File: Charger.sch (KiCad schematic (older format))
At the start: 7 parts

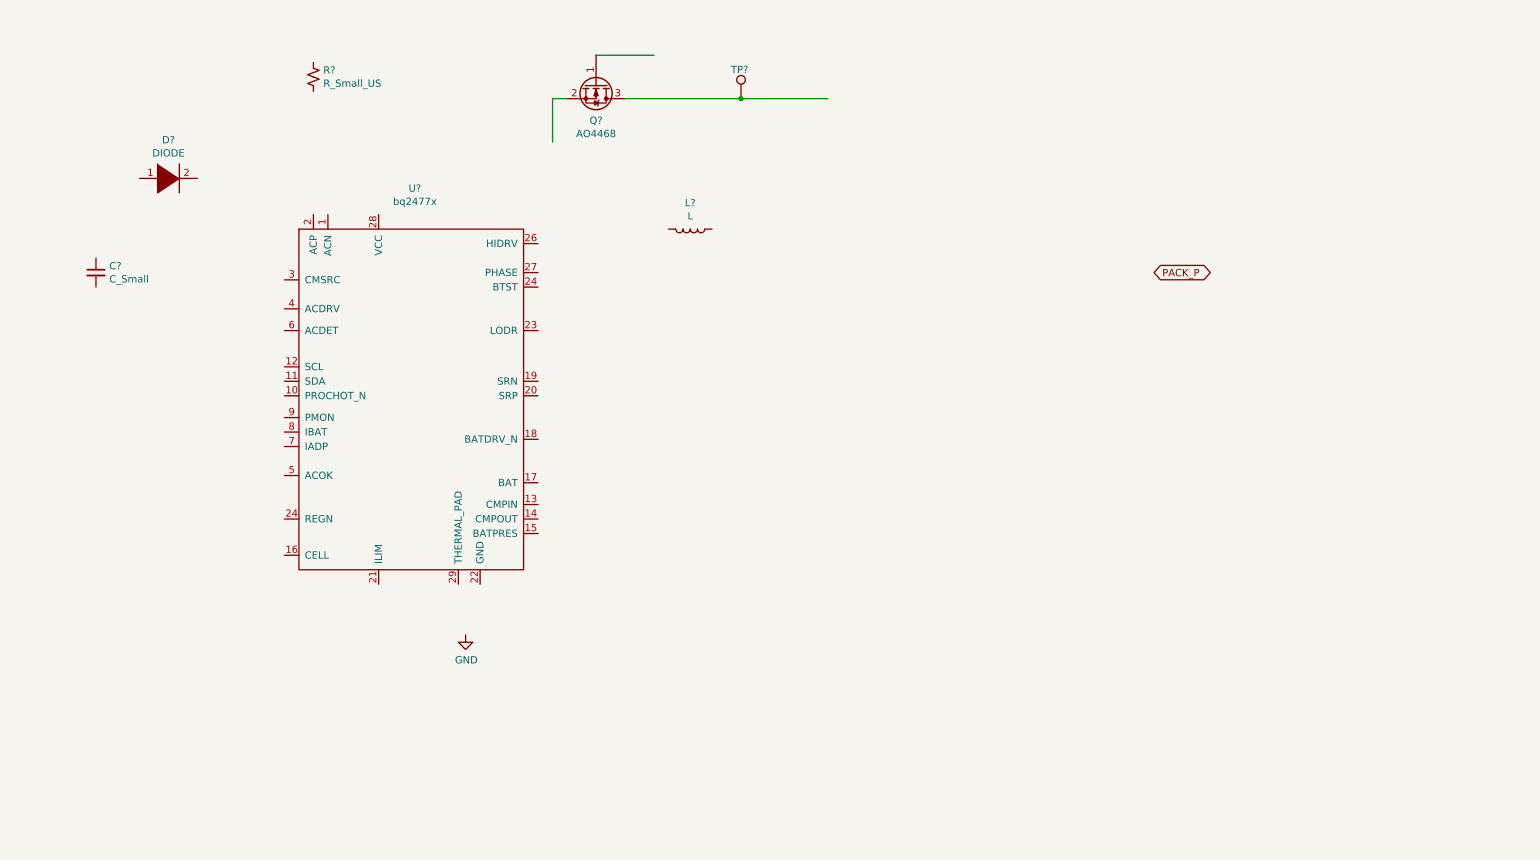
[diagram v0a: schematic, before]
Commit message: Added capacitors, inductors to charger page. Fixed capacitor sizes.
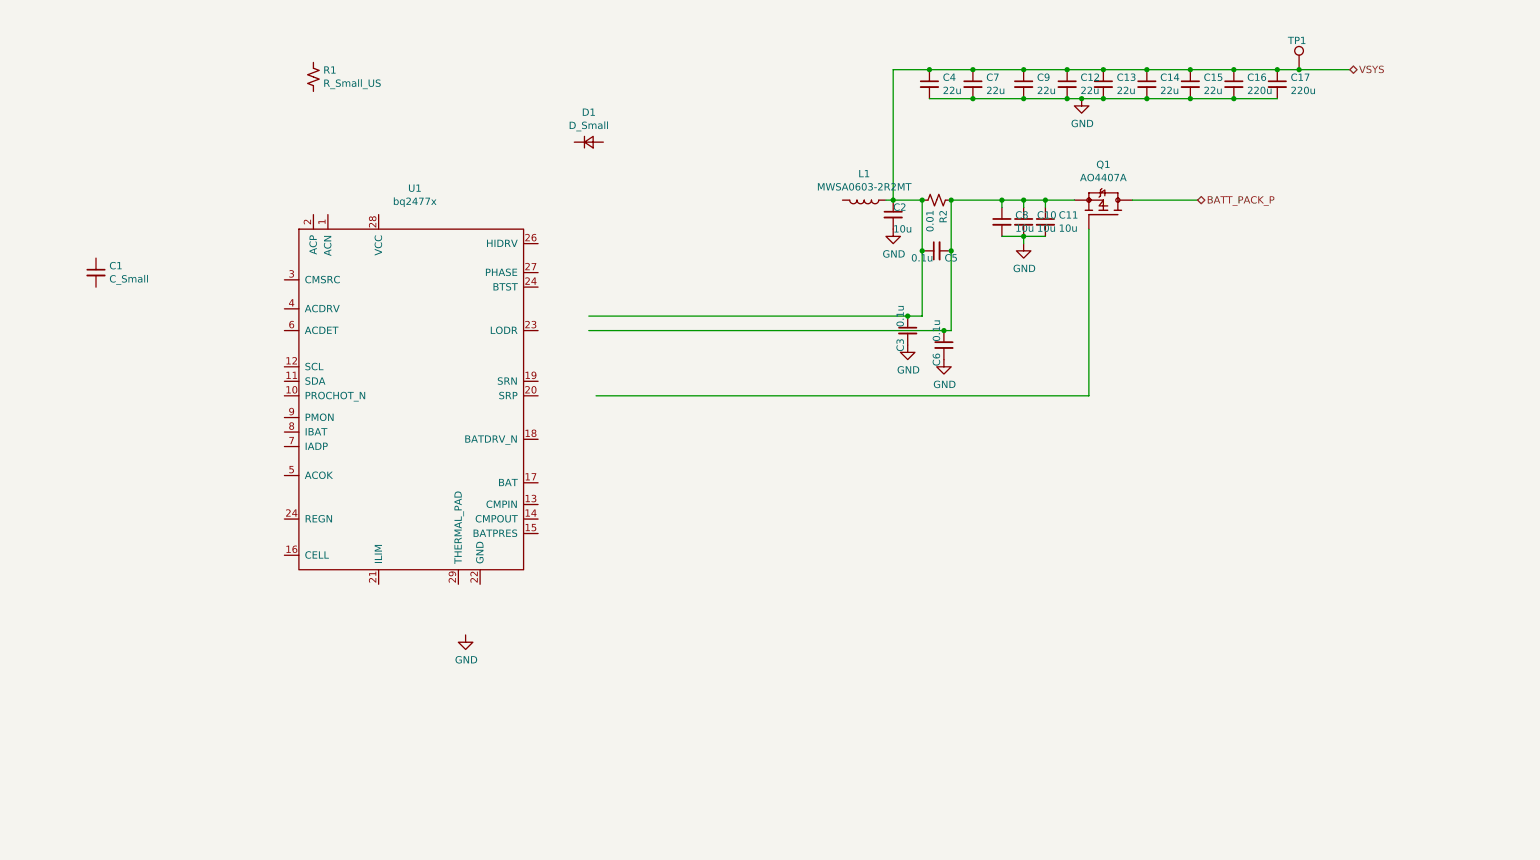
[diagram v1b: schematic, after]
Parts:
- removed D?: DIODE, symbol pspice:DIODE
- removed Q?: AO4468, Package_TO_SOT_SMD:TDSON-8-1, symbol Device:Q_NMOS_GSD
- removed TP?: TestPoint, TestPoint:TestPoint_Pad_D2.0mm, symbol Connector:TestPoint
- added C10, C11, C2, C8: 10u, Capacitor_SMD:C_0805_2012Metric, symbol Device:C_Small
- added C12, C13, C14, C15, C4, C7, C9: 22u, Capacitor_SMD:C_0805_2012Metric, symbol Device:C_Small
- added C16, C17: 220u, Capacitor_SMD:C_Elec_8x10.2, symbol Device:C_Small
- added C3, C5, C6: 0.1u, Capacitor_SMD:C_0603_1608Metric, symbol Device:C_Small
- added D1: D_Small, symbol Device:D_Small
- added Q1: AO4407A, SmartBattery:SOIC127P600X175-8N, symbol SmartBattery:AO4407A
- added R2: 0.01, Resistor_SMD:R_1206_3216Metric, symbol Device:R_Small_US
- added TP1: TestPoint, TestPoint:TestPoint_Pad_D2.0mm, symbol Connector:TestPoint
- L1: renamed from L?; value L -> MWSA0603-2R2MT; footprint (none) -> SmartBattery:MWSA0603
- U1: renamed from U?; footprint (none) -> SmartBattery:QFN40P400X400X80-29N
- gave numbers to parts that had none: 2
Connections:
- net labels added: BATT_PACK_P, VSYS
- net labels removed: PACK_P
- wire segments 5 -> 44
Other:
- moved on the sheet: L1

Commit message: Added bunch of cap to charger, made footprint for diode + fuse
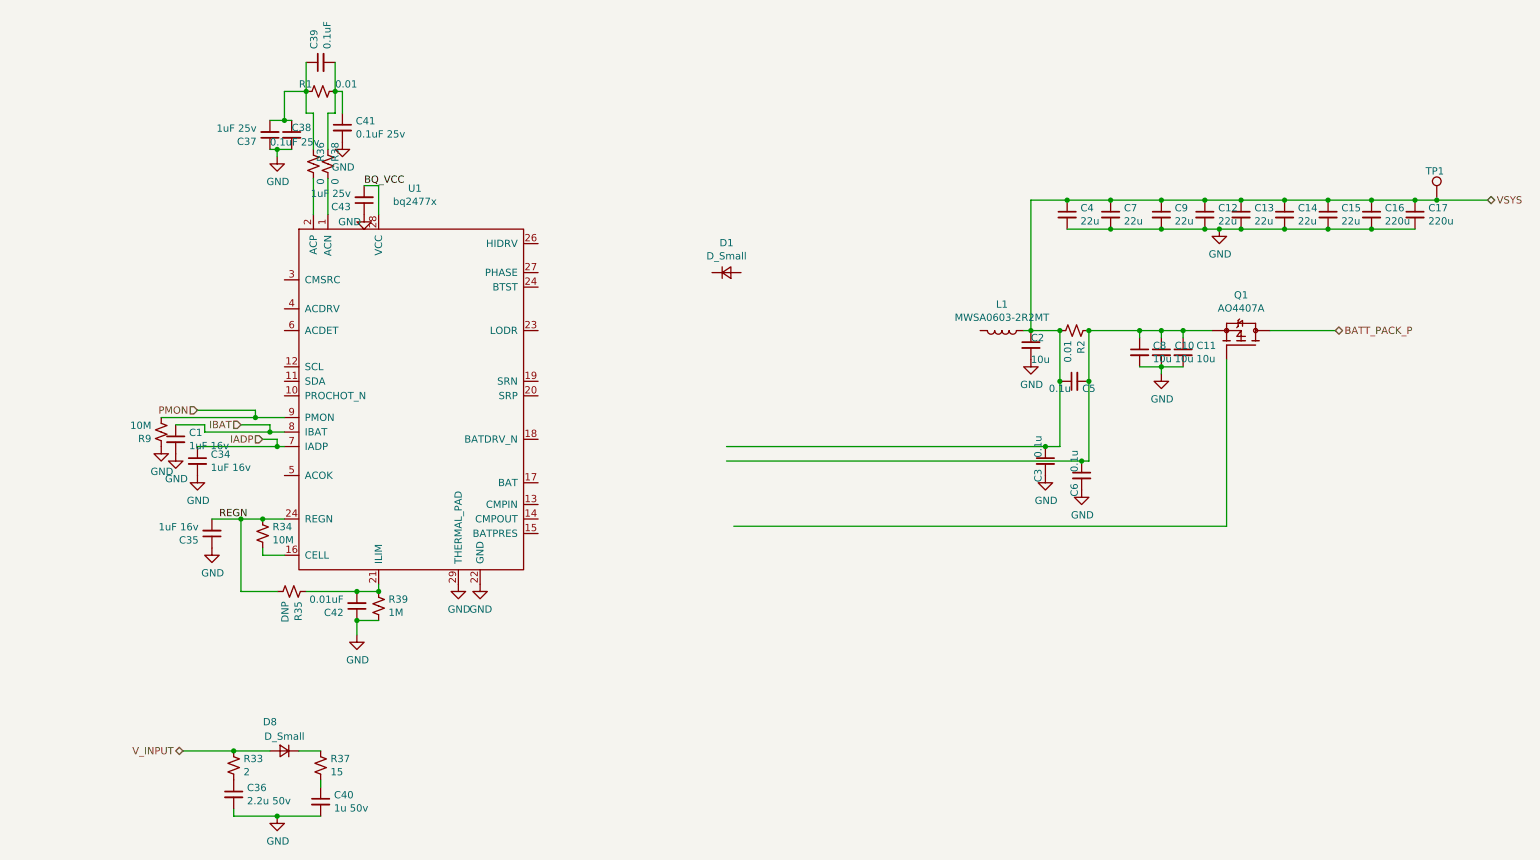
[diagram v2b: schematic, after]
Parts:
- added C34, C35: 1uF 16v, symbol Device:C_Small
- added C36: 2.2u 50v, symbol Device:C_Small
- added C37, C43: 1uF 25v, symbol Device:C_Small
- added C38, C41: 0.1uF 25v, symbol Device:C_Small
- added C39: 0.1uF, symbol Device:C_Small
- added C40: 1u 50v, symbol Device:C_Small
- added C42: 0.01uF, symbol Device:C_Small
- added D8: D_Small, symbol Device:D_Small
- added R33: 2, Resistor_SMD:R_0402_1005Metric, symbol Device:R_Small_US
- added R34: 10M, Resistor_SMD:R_0201_0603Metric, symbol Device:R_Small_US
- added R35: DNP, symbol Device:R_Small_US
- added R36, R38: 0, Resistor_SMD:R_0201_0603Metric, symbol Device:R_Small_US
- added R37: 15, Resistor_SMD:R_0402_1005Metric, symbol Device:R_Small_US
- added R39: 1M, Resistor_SMD:R_0201_0603Metric, symbol Device:R_Small_US
- added R9: 10M, Resistor_SMD:R_0402_1005Metric, symbol Device:R_Small_US
- C1: value C_Small -> 1uF 16v
- R1: value R_Small_US -> 0.01; footprint (none) -> Resistor_SMD:R_1206_3216Metric
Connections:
- net labels added: BQ_VCC, IADP, IBAT, PMON, REGN, V_INPUT
- wire segments 44 -> 98
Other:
- moved on the sheet: C10, C11, C12, C13, C14, C15, C16, C17, C2, C3, C4, C5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

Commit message: Finished Charger section, assigned all footprints. Next is output and then peripherals.
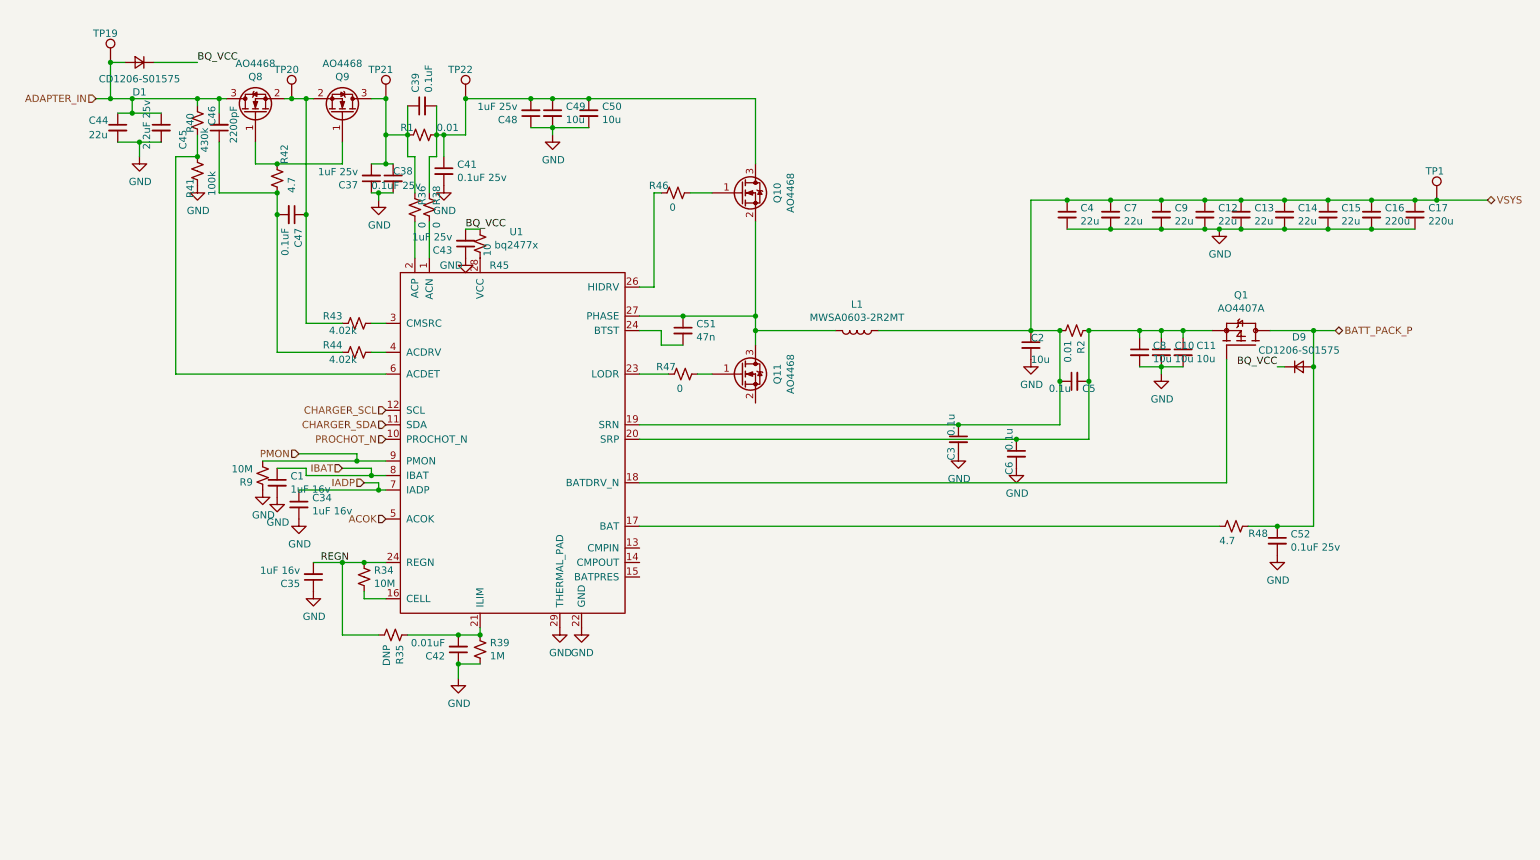
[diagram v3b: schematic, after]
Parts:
- removed C36: 2.2u 50v, symbol Device:C_Small
- removed C40: 1u 50v, symbol Device:C_Small
- removed D8: D_Small, symbol Device:D_Small
- removed R33: 2, Resistor_SMD:R_0402_1005Metric, symbol Device:R_Small_US
- removed R37: 15, Resistor_SMD:R_0402_1005Metric, symbol Device:R_Small_US
- added C44: 22u, Capacitor_SMD:C_0805_2012Metric, symbol Device:C_Small
- added C45: 2.2uF 25v, Capacitor_SMD:C_0603_1608Metric, symbol Device:C_Small
- added C46: 2200pF, Capacitor_SMD:C_0201_0603Metric, symbol Device:C_Small
- added C47: 0.1uF, Capacitor_SMD:C_0201_0603Metric, symbol Device:C_Small
- added C48: 1uF 25v, Capacitor_SMD:C_0402_1005Metric, symbol Device:C_Small
- added C49, C50: 10u, Capacitor_SMD:C_0805_2012Metric, symbol Device:C_Small
- added C51: 47n, Capacitor_SMD:C_0201_0603Metric, symbol Device:C_Small
- added C52: 0.1uF 25v, Capacitor_SMD:C_0201_0603Metric, symbol Device:C_Small
- added D9: CD1206-S01575, Diode_SMD:D_1206_3216Metric, symbol Device:D_Small
- added Q10, Q11, Q8, Q9: AO4468, Package_TO_SOT_SMD:TDSON-8-1, symbol Device:Q_NMOS_GSD
- added R40: 430k, Resistor_SMD:R_1206_3216Metric, symbol Device:R_Small_US
- added R41: 100k, Resistor_SMD:R_1206_3216Metric, symbol Device:R_Small_US
- added R42, R48: 4.7, Resistor_SMD:R_0201_0603Metric, symbol Device:R_Small_US
- added R43, R44: 4.02k, Resistor_SMD:R_0201_0603Metric, symbol Device:R_Small_US
- added R45: 10, Resistor_SMD:R_1206_3216Metric, symbol Device:R_Small_US
- added R46, R47: 0, Resistor_SMD:R_0201_0603Metric, symbol Device:R_Small_US
- added TP19, TP20, TP21, TP22: TestPoint, TestPoint:TestPoint_Pad_D2.0mm, symbol Connector:TestPoint
- C1, C34, C35, C38, C39, C41, C42: footprint (none) -> Capacitor_SMD:C_0201_0603Metric
- C37, C43: footprint (none) -> Capacitor_SMD:C_0402_1005Metric
- D1: value D_Small -> CD1206-S01575; footprint (none) -> Diode_SMD:D_1206_3216Metric
- R35: footprint (none) -> Resistor_SMD:R_0201_0603Metric
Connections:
- net labels added: ACOK, ADAPTER_IN, CHARGER_SCL, CHARGER_SDA, PROCHOT_N
- net labels removed: V_INPUT
- wire segments 98 -> 161
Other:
- moved on the sheet: C1, C3, C34, C35, C37, C38, C39, C41, C42, C43, C6, L1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

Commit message: Adding lots of changes. Started output Stage
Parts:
- removed Q10, Q11, Q8, Q9: AO4468, Package_TO_SOT_SMD:TDSON-8-1, symbol Device:Q_NMOS_GSD
- added Q10, Q11, Q8, Q9: AO4468, SmartBattery:SOIC-8_Alpha_Omega, symbol SmartBattery:AO4468
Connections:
- net ADAPTER_IN: now also Q8.5 (D), Q8.6 (D), Q8.7 (D), Q8.8 (D)
- net GND: now also Q11.1 (S), Q11.2 (S), Q11.3 (S)
- net at C51.1, L1.2, U1.27 (PHASE): now also Q10.1 (S), Q10.2 (S), Q10.3 (S), Q11.5 (D), Q11.6 (D), Q11.7 (D), Q11.8 (D)
- net at C39.2, C41.1, C48.2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: now also Q10.5 (D), Q10.6 (D), Q10.7 (D), Q10.8 (D)
- net at C37.2, C38.1, C39.1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: now also Q9.5 (D), Q9.6 (D), Q9.7 (D), Q9.8 (D)
- net at C47.1, R43.1, TP20.1: now also Q8.1 (S), Q8.2 (S), Q8.3 (S), Q9.1 (S), Q9.2 (S), Q9.3 (S)
- net at R42.1: now also Q8.4 (G), Q9.4 (G)
- net at R46.2: now also Q10.4 (G)
- net at R47.2: now also Q11.4 (G)
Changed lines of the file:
@@
 $Descr A4 11693 8268
 encoding utf-8
-Sheet 2 3
+Sheet 2 5
 Title ""
 Date ""
@@
 Wire Wire Line
 	3000 3250 2900 3250
-$Comp
-L Device:Q_NMOS_GSD Q?
-U 1 1 5FECA337
-P 2100 1600
-AR Path="/5FD15753/5FECA337" Ref="Q?"  Part="1"
-AR Path="/5FD99B08/5FECA337" Ref="Q8"  Part="1"
-F 0 "Q8" V 2351 1600 50  0000 C CNN
-F 1 "AO4468" V 2442 1600 50  0000 C CNN
-F 2 "Package_TO_SOT_SMD:TDSON-8-1" H 2300 1700 50  0001 C CNN
-F 3 "~" H 2100 1600 50  0001 C CNN
-	1    2100 1600
-	0    -1   -1   0
-$EndComp
-$Comp
-L Device:Q_NMOS_GSD Q?
-U 1 1 5FEF377C
-P 2700 1600
-AR Path="/5FD15753/5FEF377C" Ref="Q?"  Part="1"
-AR Path="/5FD99B08/5FEF377C" Ref="Q9"  Part="1"
-F 0 "Q9" V 2951 1600 50  0000 C CNN
-F 1 "AO4468" V 3042 1600 50  0000 C CNN
-F 2 "Package_TO_SOT_SMD:TDSON-8-1" H 2900 1700 50  0001 C CNN
-F 3 "~" H 2700 1600 50  0001 C CNN
-	1    2700 1600
-	0    1    -1   0
-$EndComp
 Wire Wire Line
 	2300 1500 2350 1500
@@
 Wire Wire Line
 	4400 1700 4150 1700
-$Comp
-L Device:Q_NMOS_GSD Q?
-U 1 1 5FFB61C9
-P 5450 2150
-AR Path="/5FD15753/5FFB61C9" Ref="Q?"  Part="1"
-AR Path="/5FD99B08/5FFB61C9" Ref="Q10"  Part="1"
-F 0 "Q10" V 5701 2150 50  0000 C CNN
-F 1 "AO4468" V 5792 2150 50  0000 C CNN
-F 2 "Package_TO_SOT_SMD:TDSON-8-1" H 5650 2250 50  0001 C CNN
-F 3 "~" H 5450 2150 50  0001 C CNN
-	1    5450 2150
-	1    0    0    -1
-$EndComp
-$Comp
-L Device:Q_NMOS_GSD Q?
-U 1 1 5FFC22FA
-P 5450 3400
-AR Path="/5FD15753/5FFC22FA" Ref="Q?"  Part="1"
-AR Path="/5FD99B08/5FFC22FA" Ref="Q11"  Part="1"
-F 0 "Q11" V 5701 3400 50  0000 C CNN
-F 1 "AO4468" V 5792 3400 50  0000 C CNN
-F 2 "Package_TO_SOT_SMD:TDSON-8-1" H 5650 3500 50  0001 C CNN
-F 3 "~" H 5450 3400 50  0001 C CNN
-	1    5450 3400
-	1    0    0    -1
-$EndComp
 Wire Wire Line
 	4850 2800 4850 2150
@@
 	1    0    0    -1
 $EndComp
+$Comp
+L SmartBattery:AO4468 Q8
+U 1 1 6038DB58
+P 2100 1600
+F 0 "Q8" V 2443 1600 50  0000 C CNN
+F 1 "AO4468" V 2352 1600 50  0000 C CNN
+F 2 "SmartBattery:SOIC-8_Alpha_Omega" H 2300 1700 50  0001 C CNN
+F 3 "~" H 2100 1600 50  0001 C CNN
+	1    2100 1600
+	0    -1   -1   0
+$EndComp
+$Comp
+L SmartBattery:AO4468 Q9
+U 1 1 60390F2A
+P 2700 1600
+F 0 "Q9" V 3043 1600 50  0000 C CNN
+F 1 "AO4468" V 2952 1600 50  0000 C CNN
+F 2 "SmartBattery:SOIC-8_Alpha_Omega" H 2900 1700 50  0001 C CNN
+F 3 "~" H 2700 1600 50  0001 C CNN
+	1    2700 1600
+	0    1    -1   0
+$EndComp
+$Comp
+L SmartBattery:AO4468 Q10
+U 1 1 603A12F1
+P 5450 2150
+F 0 "Q10" H 5656 2196 50  0000 L CNN
+F 1 "AO4468" H 5656 2105 50  0000 L CNN
+F 2 "SmartBattery:SOIC-8_Alpha_Omega" H 5650 2250 50  0001 C CNN
+F 3 "~" H 5450 2150 50  0001 C CNN
+	1    5450 2150
+	1    0    0    -1
+$EndComp
+$Comp
+L SmartBattery:AO4468 Q11
+U 1 1 603A292B
+P 5450 3400
+F 0 "Q11" H 5656 3446 50  0000 L CNN
+F 1 "AO4468" H 5656 3355 50  0000 L CNN
+F 2 "SmartBattery:SOIC-8_Alpha_Omega" H 5650 3500 50  0001 C CNN
+F 3 "~" H 5450 3400 50  0001 C CNN
+	1    5450 3400
+	1    0    0    -1
+$EndComp
+$Comp
+L power:GND #PWR0144
+U 1 1 6041593B
+P 5550 3600
+F 0 "#PWR0144" H 5550 3350 50  0001 C CNN
+F 1 "GND" H 5555 3427 50  0000 C CNN
+F 2 "" H 5550 3600 50  0001 C CNN
+F 3 "" H 5550 3600 50  0001 C CNN
+	1    5550 3600
+	1    0    0    -1
+$EndComp
